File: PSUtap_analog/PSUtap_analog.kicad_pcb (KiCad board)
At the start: 2 copper layers, 152.4 x 73.7 mm, 58 parts, among them J1 Conn_to_digital_board, U1 AD7708, U2 LT6105, U3 LT6105, U4 LT6105, U5 LT6105, U6 LT6105

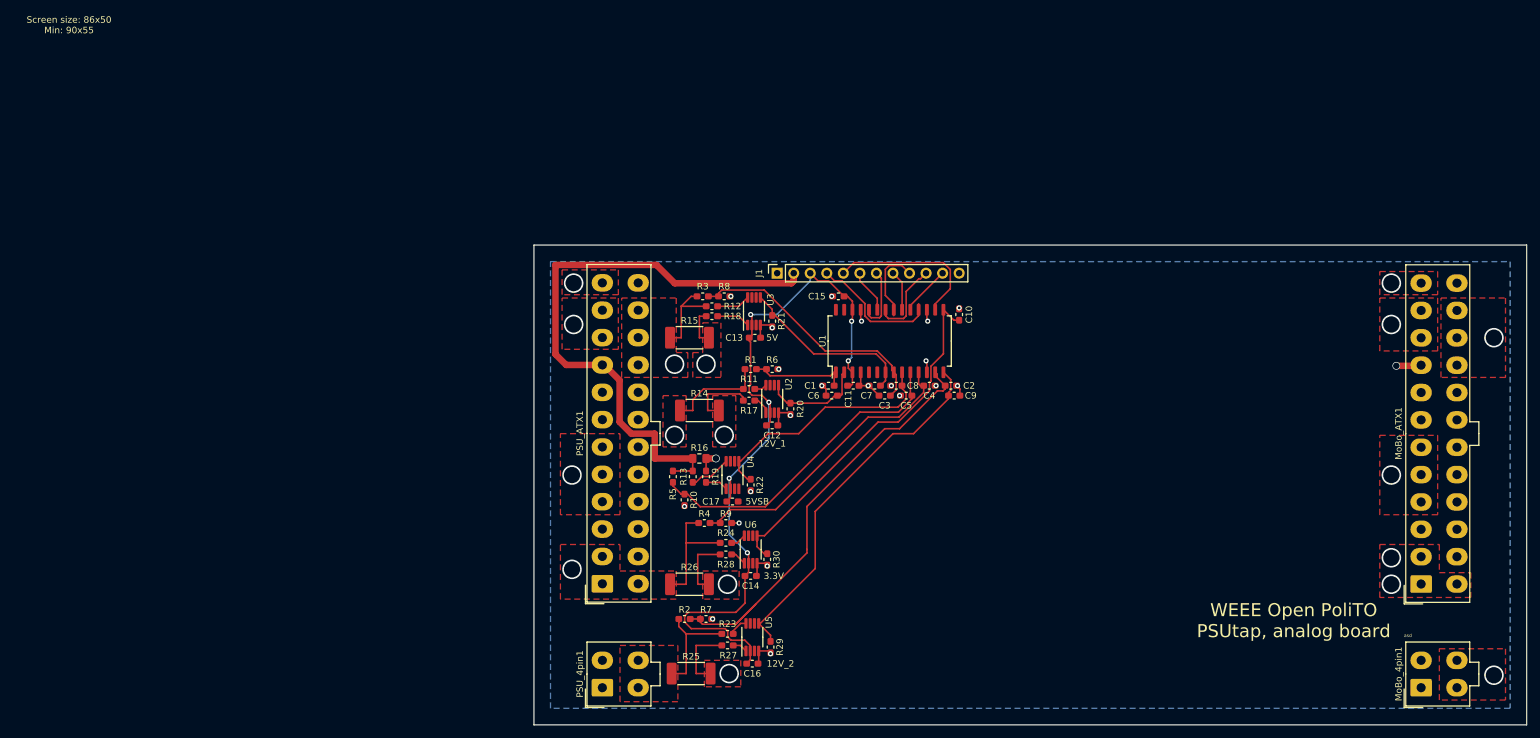
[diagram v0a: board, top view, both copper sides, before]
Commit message: Updated analog board PCB and started digital board PSB
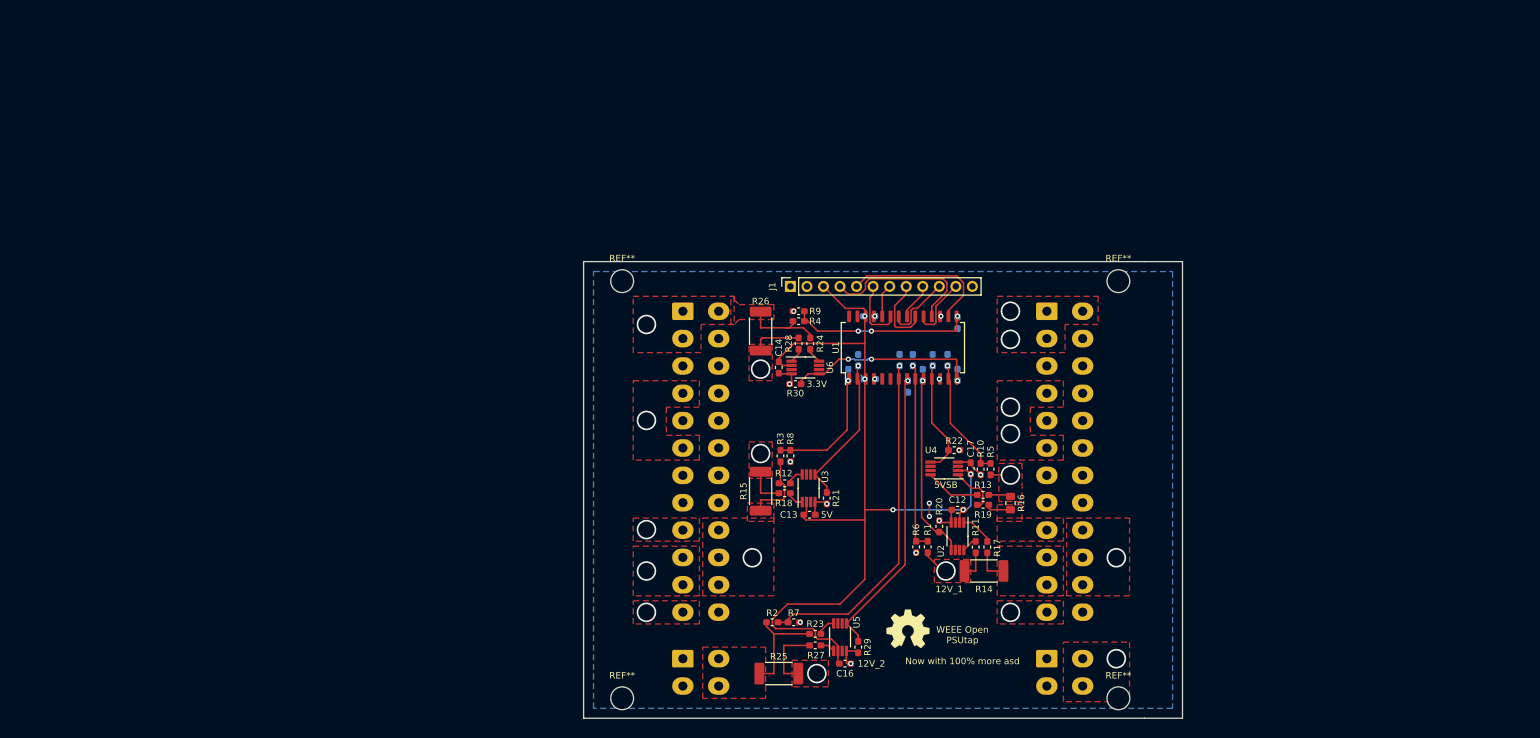
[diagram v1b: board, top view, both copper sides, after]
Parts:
- added REF**: MountingHole_2.5mm, MountingHole:MountingHole_2.5mm, F.Cu at (183.7, 117.8)
- added REF**: MountingHole_2.5mm, MountingHole:MountingHole_2.5mm, F.Cu at (107.5, 117.8)
- added REF**: MountingHole_2.5mm, MountingHole:MountingHole_2.5mm, F.Cu at (183.7, 53.8)
- added REF**: MountingHole_2.5mm, MountingHole:MountingHole_2.5mm, F.Cu at (107.5, 53.8)
- added REF**: OSHW-Symbol_6.7x6mm_SilkScreen, Symbol:OSHW-Symbol_6.7x6mm_SilkScreen, F.Cu at (151.4, 107.2)
- C1, C10, C11, C15, C2, C3, C4, C5, C6, C7, C8, C9, MoBo_4pin1, MoBo_ATX1, PSU_4pin1, PSU_ATX1: moved to B.Cu
- moved MoBo_ATX1 71.1 mm to (172.7, 58.4), turned to 270 degrees
- moved MoBo_4pin1 57.6 mm to (172.7, 111.8), turned to 270 degrees
- moved R14 50.2 mm to (163.1, 98.3)
- moved R5 48.8 mm to (164.1, 82.7), turned to 90 degrees
- moved R16 48.2 mm to (167.1, 87.9), turned to 270 degrees
- moved R10 45.7 mm to (162.6, 82.7)
- moved R13 44.7 mm to (162.9, 86.6), turned to 0 degrees
- moved PSU_ATX1 43.6 mm to (116.8, 58.4), turned to 270 degrees
- moved R17 42.9 mm to (163.6, 94.6), turned to 90 degrees
- moved R19 42.7 mm to (162.9, 88.1), turned to 180 degrees
- moved R11 42.4 mm to (161.8, 94.6), turned to 270 degrees
- moved R26 40.4 mm to (128.8, 61.5), turned to 270 degrees
- moved R1 38.5 mm to (154.4, 94.6), turned to 90 degrees
- moved C17 36.9 mm to (161.0, 82.5), turned to 90 degrees
- moved U2 35.4 mm to (159.0, 93.0), turned to 270 degrees
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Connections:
- C1 pad 1: /A7 -> /A3
- C10 pad 1: /A6 -> /A10
- C2 pad 1: /A9 -> /A1
- C3 pad 1: /A2 -> /A7
- C4 pad 1: /A5 -> /A6
- C5 pad 1: /A4 -> /A9
- C6 pad 1: /A8 -> /A4
- C7 pad 1: /A1 -> /A8
- C8 pad 1: /A3 -> /A5
- C9 pad 1: /A10 -> /A2
- R1 pad 2: /A7 -> /A3
- R10 pad 1: /A4 -> /A9
- R2 pad 2: /A9 -> /A1
- R20 pad 1: /A8 -> /A4
- R21 pad 1: /A1 -> /A8
- R22 pad 1: /A3 -> /A5
- R29 pad 1: /A10 -> /A2
- R3 pad 2: /A2 -> /A7
- R30 pad 1: /A6 -> /A10
- R4 pad 2: /A5 -> /A6
- R5 pad 2: /A4 -> /A9
- R6 pad 1: /A7 -> /A3
- R7 pad 1: /A9 -> /A1
- R8 pad 1: /A2 -> /A7
- R9 pad 1: /A5 -> /A6
- U2 pad 5: /A8 -> /A4
- U3 pad 5: /A1 -> /A8
- U4 pad 5: /A3 -> /A5
- U5 pad 5: /A10 -> /A2
- U6 pad 5: /A6 -> /A10
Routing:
- net /5VSB_tap: track 91.5 -> 6.49 mm, vias 0 -> 2
- net /A9: track 67.3 -> 18.6 mm, vias 0 -> 1
- net /A6: track 55.8 -> 27.7 mm, vias 0 -> 3
- net /A10: track 56.7 -> 28.8 mm, vias 0 -> 3
- net /A5: track 45.1 -> 17.9 mm, vias 0 -> 1
- net /A1: track 27.7 -> 53.4 mm, vias 0 -> 1
- net /A4: track 49.6 -> 28.8 mm, vias 0 -> 1
- net /5Vsup: track 119.5 -> 137.5 mm, vias 6 -> 5
- net /A3: track 37.8 -> 28.9 mm, vias 0 -> 1
- net GND: track 31.4 -> 22.6 mm, vias 21 -> 16
- net /A8: track 15.8 -> 23.7 mm, vias 0 -> 1
- net Net-(J1-Pad9): track 12.1 -> 5.60 mm
- net /12V1_tap: track 15.2 -> 8.78 mm
- net /A2: track 38.9 -> 45.2 mm, vias 0 -> 1
- net /3.3V_tap: track 19.0 -> 12.9 mm
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- added copper zone on F.Cu, net /5VSB_mobo
- added copper zone on F.Cu, net /5VSB_tap
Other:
- board size 152.4 x 73.7 mm -> 91.9 x 70.1 mm
- board text added: "IN"
- board text added: "OUT"
- board text added: "WEEE Open PSUtap Now with 100% more asd"
- board text removed: "Screen size: 86x50 Min: 90x55"
- board text removed: "WEEE Open PoliTO PSUtap, analog board"
- board text removed: "asd"

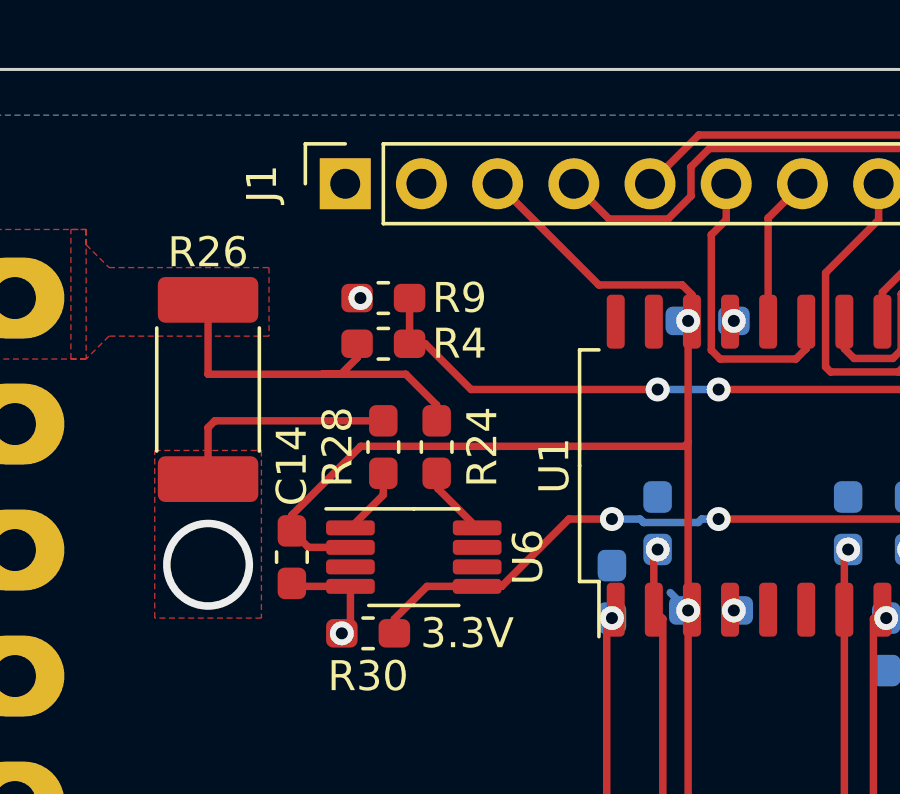
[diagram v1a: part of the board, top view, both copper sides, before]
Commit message: Removed PCB copies, added xtal to ADC in analog board, finished digital board's PCB
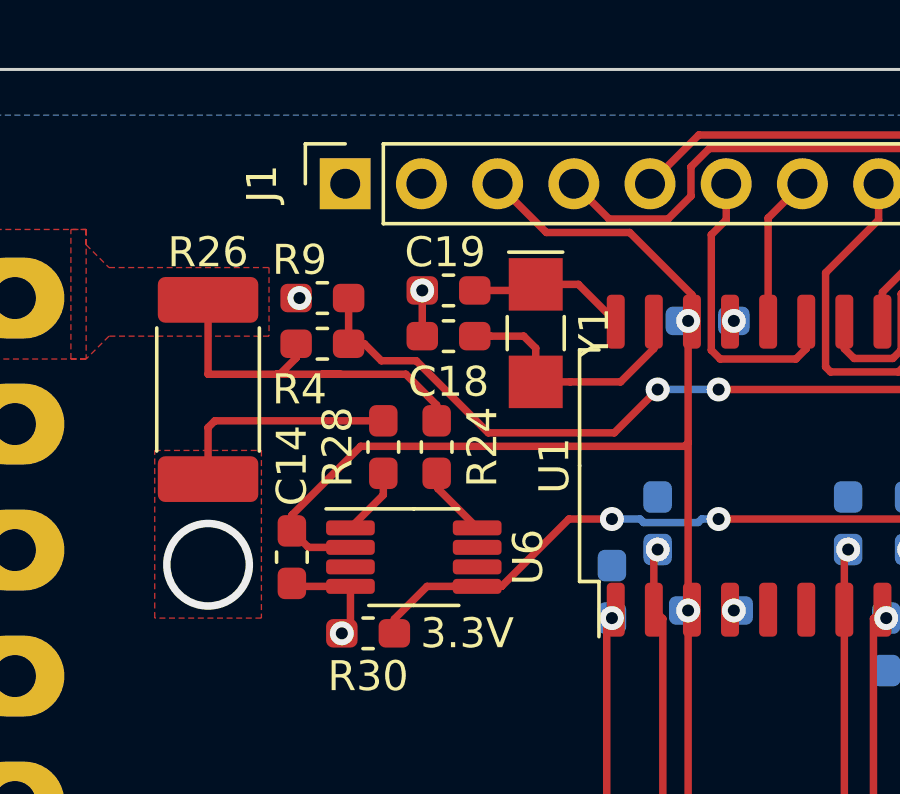
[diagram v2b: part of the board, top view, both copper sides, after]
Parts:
- added C18: 10p, Capacitor_SMD:C_0603_1608Metric_Pad1.05x0.95mm_HandSolder, F.Cu at (136.8, 59.7)
- added C19: 10p, Capacitor_SMD:C_0603_1608Metric_Pad1.05x0.95mm_HandSolder, F.Cu at (136.8, 58.2)
- added Y1: 32.768kHz, Crystal:Crystal_SMD_EuroQuartz_EQ161-2Pin_3.2x1.5mm_HandSoldering, F.Cu at (139.7, 59.6)
- moved R4 2.03 mm to (132.6, 59.9)
- moved R9 2.03 mm to (132.6, 58.4)
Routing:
- net Net-(C18-Pad2): track 0.00 -> 8.62 mm
- net Net-(C19-Pad1): track 0.00 -> 5.30 mm
- net /A6: track 27.7 -> 31.0 mm
- net GND: track 22.6 -> 24.2 mm, vias 16 -> 17
- net /5Vsup: track 137.5 -> 136.6 mm

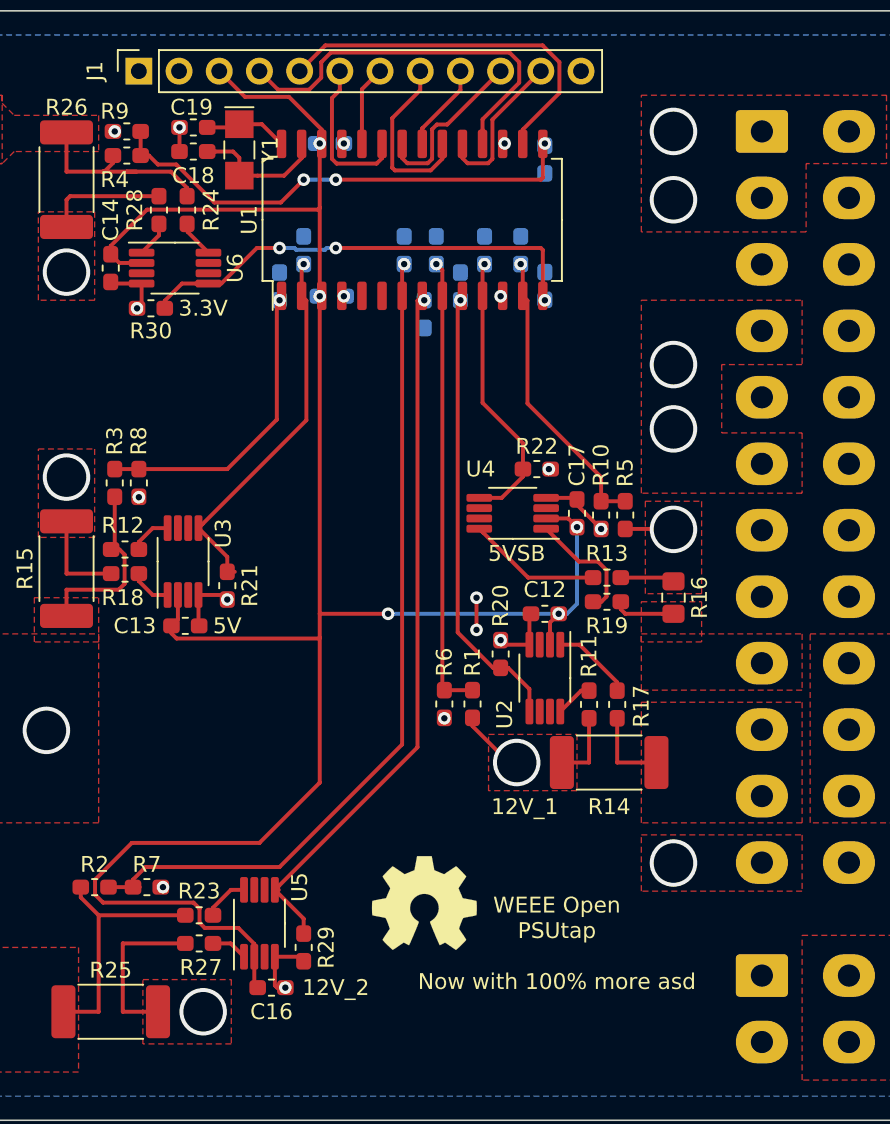
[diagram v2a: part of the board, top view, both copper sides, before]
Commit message: Updated PCBs to not have vias on component pads
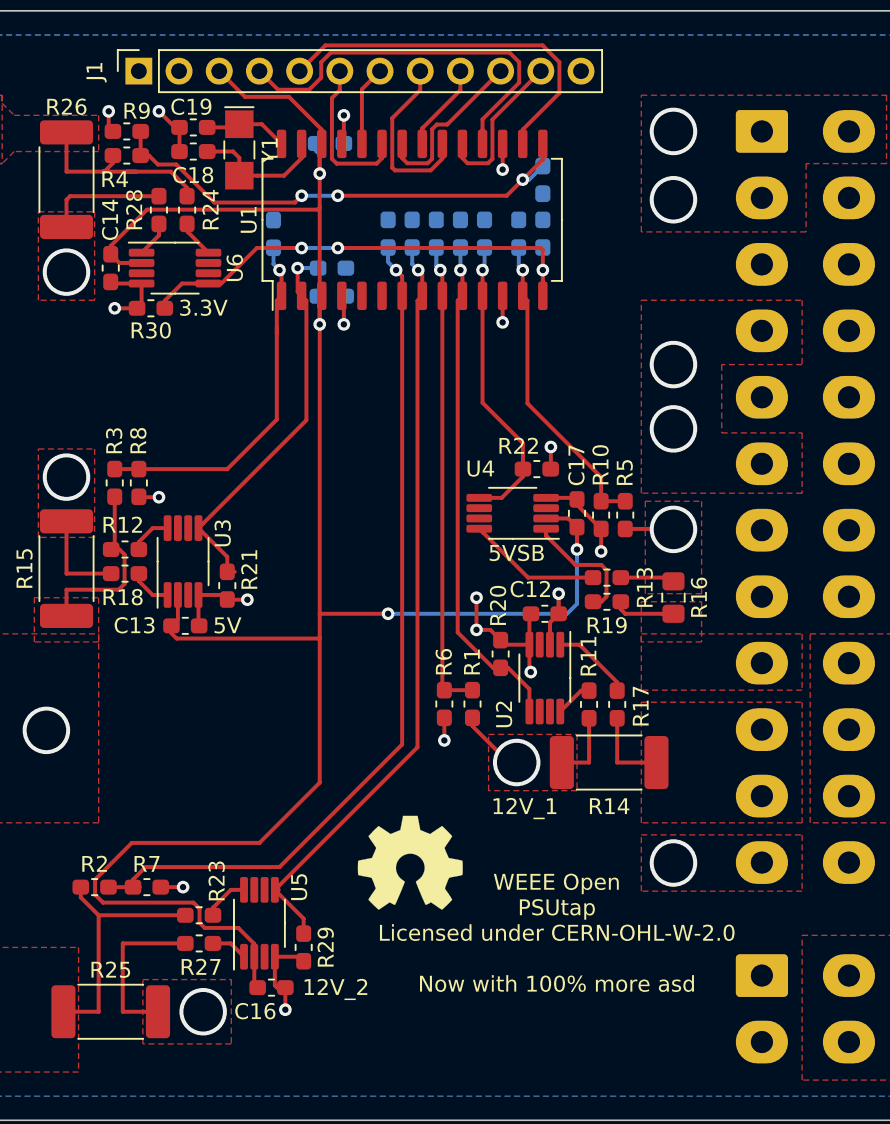
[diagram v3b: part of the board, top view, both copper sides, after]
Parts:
- moved C9 5.14 mm to (150.6, 64.9), turned to 90 degrees
- moved C3 3.34 mm to (141.9, 64.9)
- moved C6 3.33 mm to (153.7, 64.9)
- moved C10 3.30 mm to (158.9, 64.9)
- moved REF** 2.69 mm to (150.5, 104.6)
- moved C7 2.12 mm to (145.6, 67.1), turned to 0 degrees
- moved C2 1.46 mm to (149.1, 64.9)
- moved C4 1.29 mm to (158.9, 61.5)
- moved C5 1.05 mm to (157.4, 64.9)
- moved C1 1.04 mm to (152.1, 64.9)
- moved C8 1.04 mm to (155.2, 64.9)
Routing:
- net GND: track 24.2 -> 48.9 mm
- net /5Vsup: track 136.6 -> 142.9 mm
- net /A7: track 19.5 -> 23.1 mm
- net /A2: track 45.2 -> 48.5 mm
- net /A4: track 28.8 -> 31.9 mm
- net /A1: track 53.4 -> 54.8 mm
- net /A9: track 18.6 -> 19.7 mm
- net /A8: track 23.7 -> 24.8 mm
- net /A3: track 28.9 -> 30.0 mm
- net /A5: track 17.9 -> 18.9 mm
- net /A6: track 31.0 -> 31.9 mm
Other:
- board text added: "WEEE Open PSUtap Licensed under CERN-OHL-W-2.0 Now with 100% more asd"
- board text removed: "WEEE Open PSUtap Now with 100% more asd"
